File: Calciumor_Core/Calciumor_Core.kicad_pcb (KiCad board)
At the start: 2 copper layers, 77 x 145 mm, 127 parts, among them J1 OLED, J2 USB_C_Main, Q2 2SC4116, Q3 2SC4116, SW1 SW_Push, SW10 SW_Push, SW11 SW_Push, SW12 SW_Push, SW13 SW_Push, SW14 SW_Push, SW15 SW_Push, SW16 SW_Push, SW17 SW_Push, SW18 SW_Push, SW19 TMHU27, SW2 SW_Push, SW20 Power_SW, SW21 Program, SW22 Reset, SW3 SW_Push, SW4 RotaryEncoder_Switch, SW5 SW_Push, SW6 SW_Push, SW7 SW_Push, SW8 SW_Push, SW9 SW_Push, U1 LM324APT, U2 NJM12877F25, U3 ESP32-S3-WROOM-1-N16R8, U4 MCP73831-2-OT, U5 BD5229G-1, U6 NC7SV157, U7 FT231XS, U8 XC6194AA03ER-G, U9 AE-XC9306-3V3

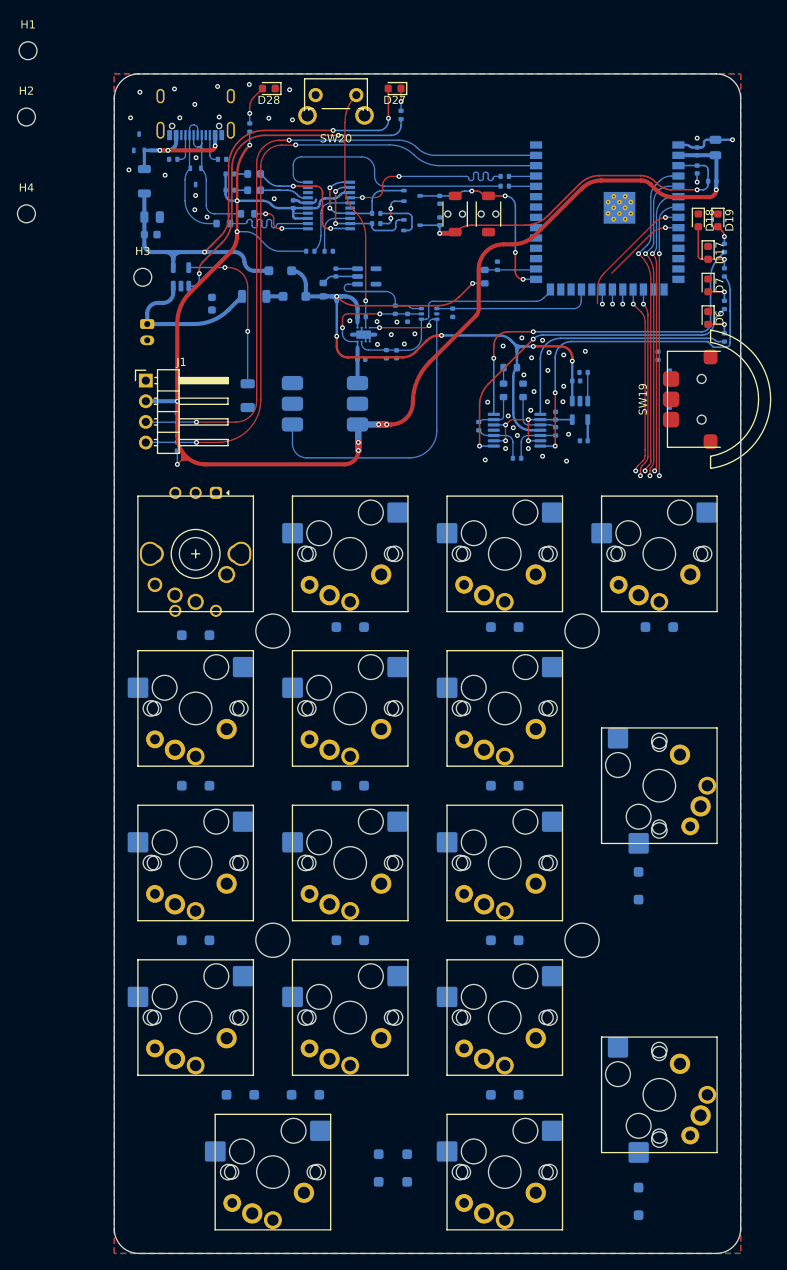
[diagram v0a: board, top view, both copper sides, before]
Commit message: Changed to socket switch type
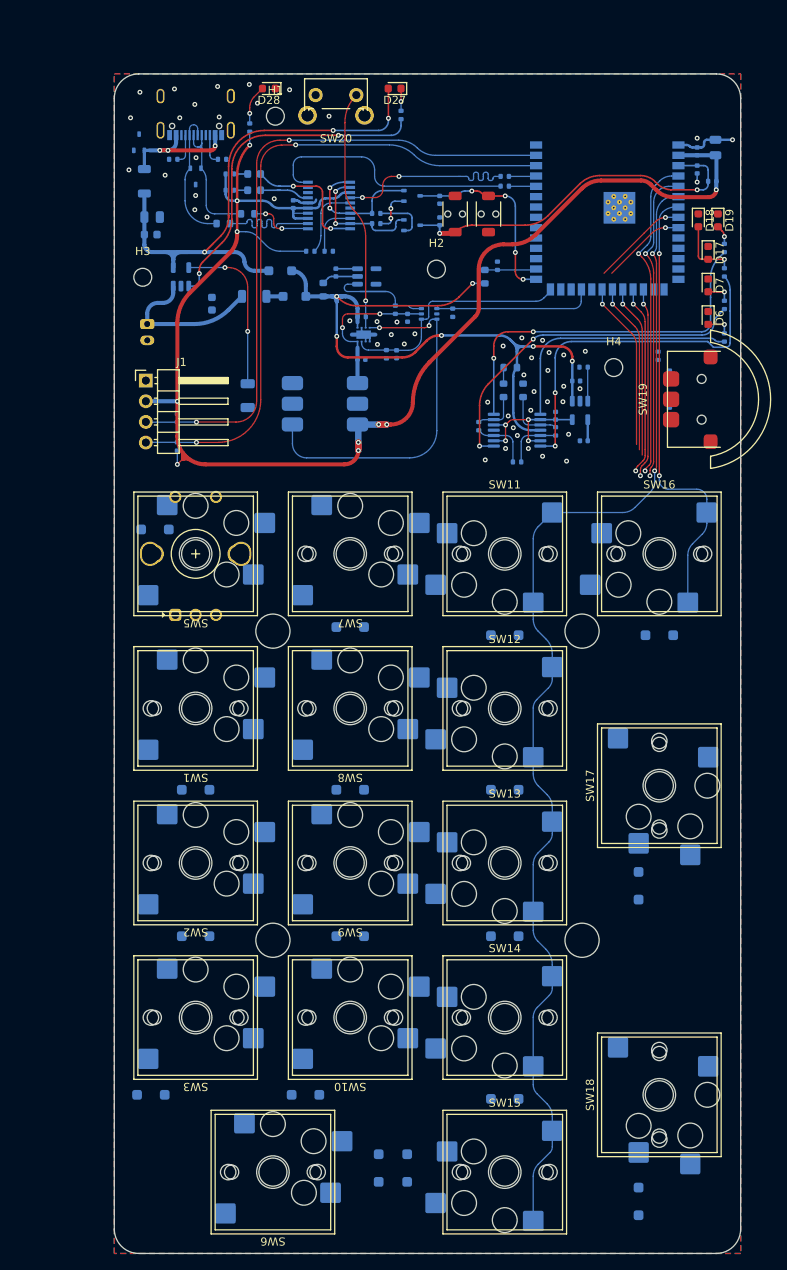
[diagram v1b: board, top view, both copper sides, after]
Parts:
- SW1, SW10, SW11, SW12, SW13, SW14, SW15, SW16, SW17, SW18, SW2, SW3, SW5, SW6, SW7, SW8, SW9: footprint Ultramarine-2:MX-Kailh -> Calciumor:MX_Choc_Socket
- moved H4 74.6 mm to (131.4, 71.1)
- moved H2 53.8 mm to (109.6, 59.0)
- moved H1 31.4 mm to (89.8, 40.2)
- moved D1 13.9 mm to (75.0, 91.0)
- moved D4 11.0 mm to (74.5, 160.5)
- moved D12 1.00 mm to (118.0, 104.0)
- moved D20 1.00 mm to (137.0, 104.0)
- moved R9 0.65 mm to (127.7, 71.0)
- moved D10 0.50 mm to (99.0, 141.0)
- moved D13 0.50 mm to (118.0, 123.0)
- moved D14 0.50 mm to (118.0, 141.0)
- moved D15 0.50 mm to (118.0, 161.0)
- moved D2 0.50 mm to (80.0, 123.0)
- moved D3 0.50 mm to (80.0, 141.0)
- moved D9 0.50 mm to (99.0, 123.0)
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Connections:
- SW4 pad S1: Net-(D1-A) -> /C0
- SW4 pad S2: /C0 -> Net-(D1-A)
- U3 pad 8: /RE_B -> /RE_A
- U3 pad 9: /RE_A -> /RE_B
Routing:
- net /C2: track 35.8 -> 145.8 mm
- net /C3: track 34.8 -> 55.9 mm
- net /R2: track 1.80 -> 21.2 mm
- net /R3: track 1.87 -> 21.0 mm
- net /R4: track 1.88 -> 20.8 mm
- net /RE_B: track 15.9 -> 10.4 mm
- net /RE_A: track 10.4 -> 11.9 mm
- net Net-(U2-CTRL): track 3.52 -> 4.17 mm
- net GND: vias 52 -> 53
